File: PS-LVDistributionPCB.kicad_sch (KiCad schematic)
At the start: 1 part, among them J15 Conn_01x20

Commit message: common gnd
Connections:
- net GND2 is gone; now on net GND: J15.16 (Pin_16)
- net GND3 is gone; now on net GND: J15.17 (Pin_17)
- net GND4 is gone; now on net GND: J15.18 (Pin_18)
- net GND5 is gone; now on net GND: J15.19 (Pin_19)
- net GND6 is gone; now on net GND: J15.20 (Pin_20)
- net GND1 renamed GND

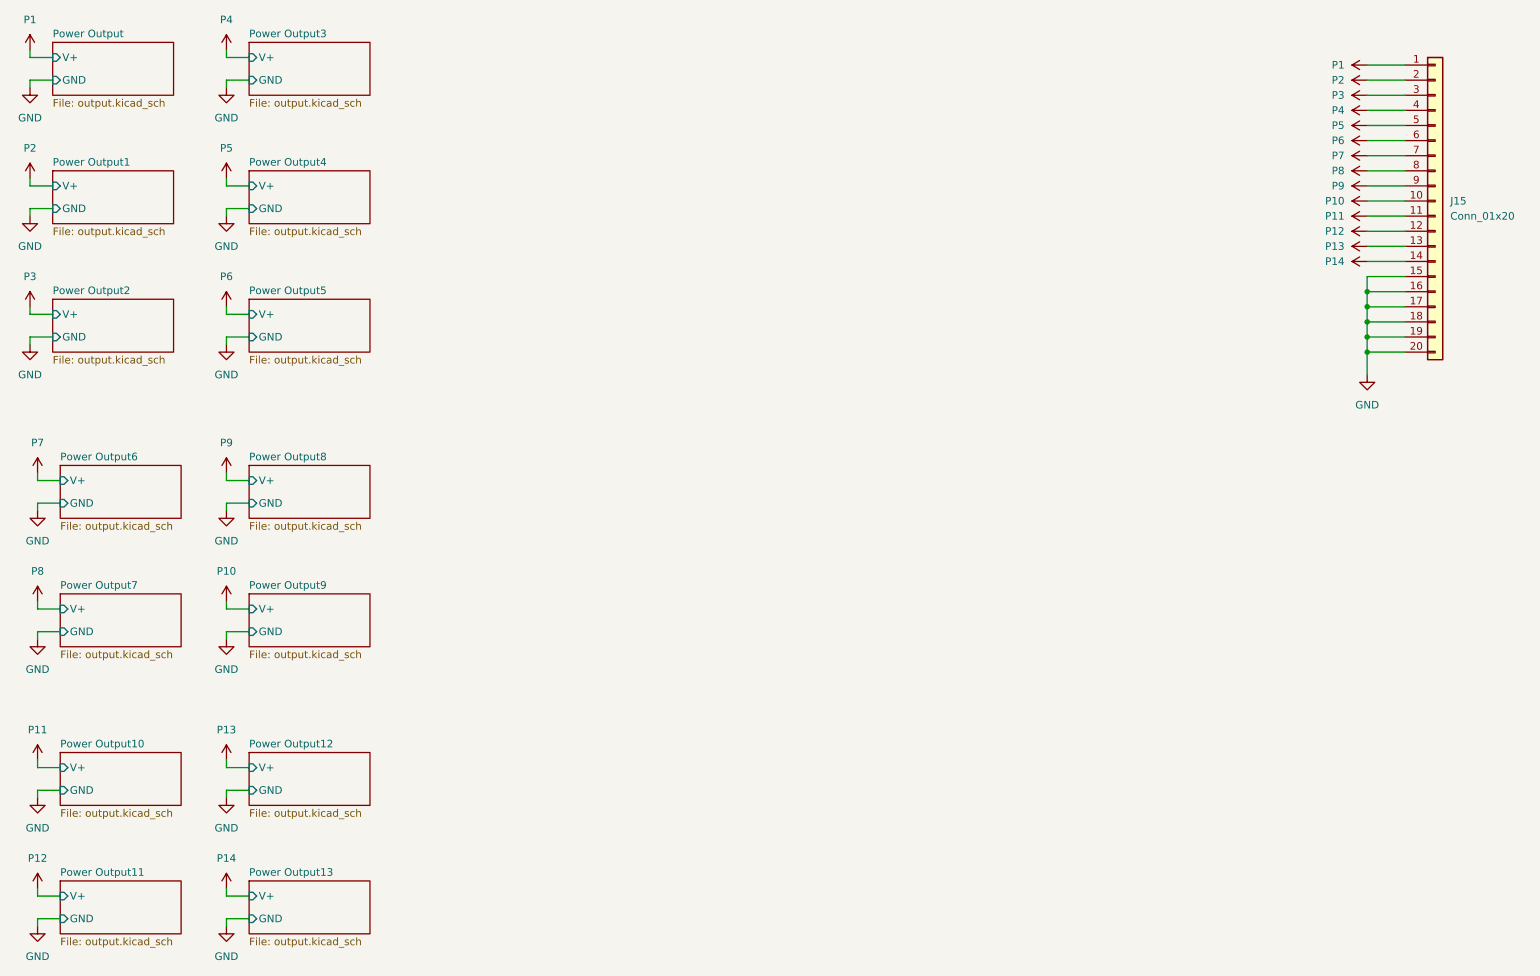
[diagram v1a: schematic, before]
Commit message: removed 2 outputs + smaller
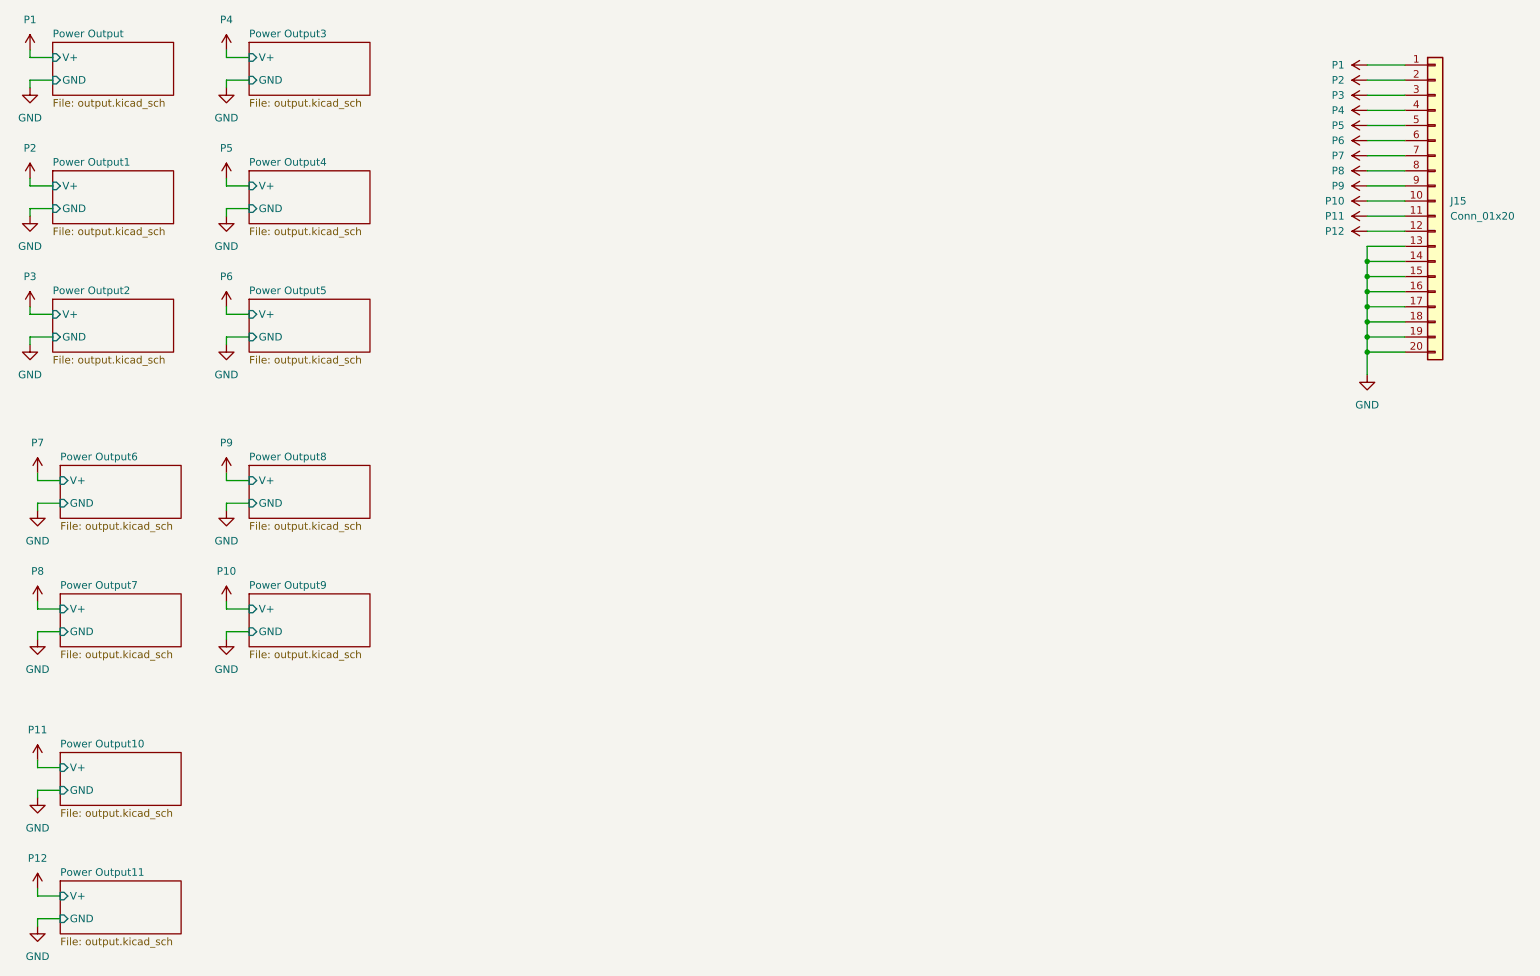
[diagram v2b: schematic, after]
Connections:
- net P13 is gone; now on net GND: J15.13 (Pin_13)
- net P14 is gone; now on net GND: J15.14 (Pin_14)
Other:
- removed sheet Power Output12
- removed sheet Power Output13
